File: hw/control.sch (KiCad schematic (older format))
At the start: 12 parts

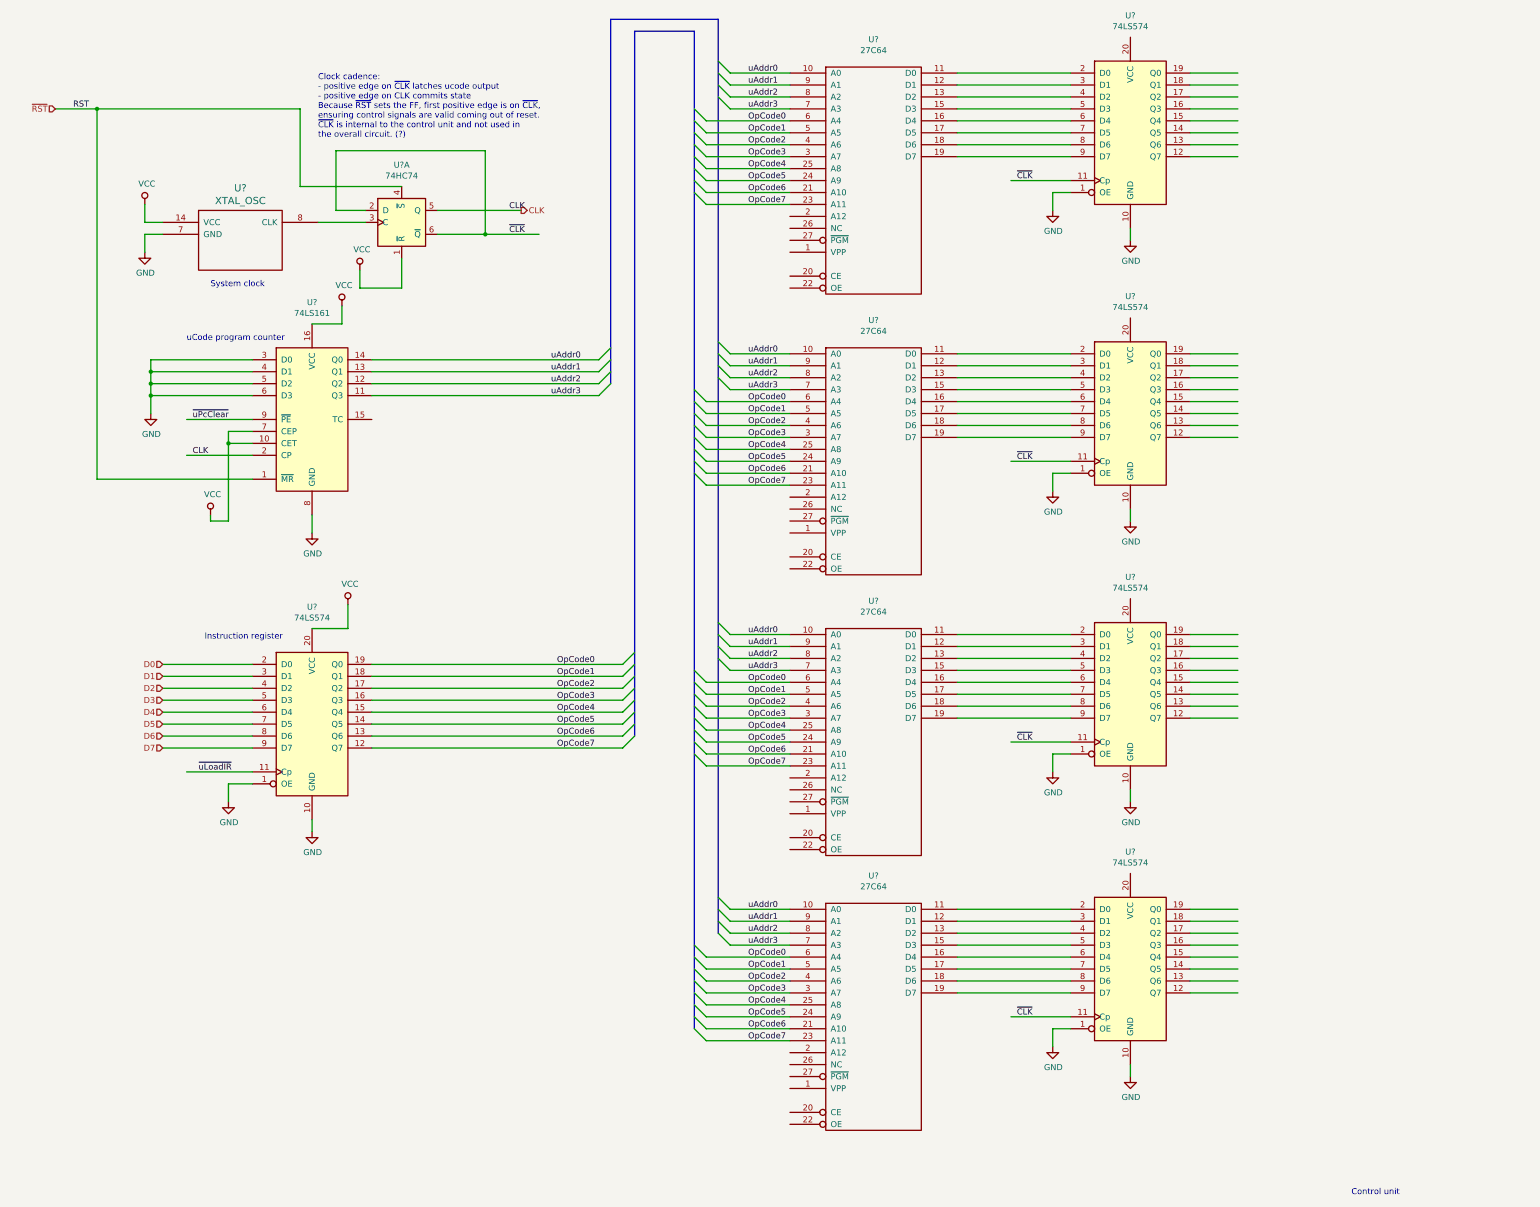
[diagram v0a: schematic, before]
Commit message: annotate control schematic, add other 74HC74 units
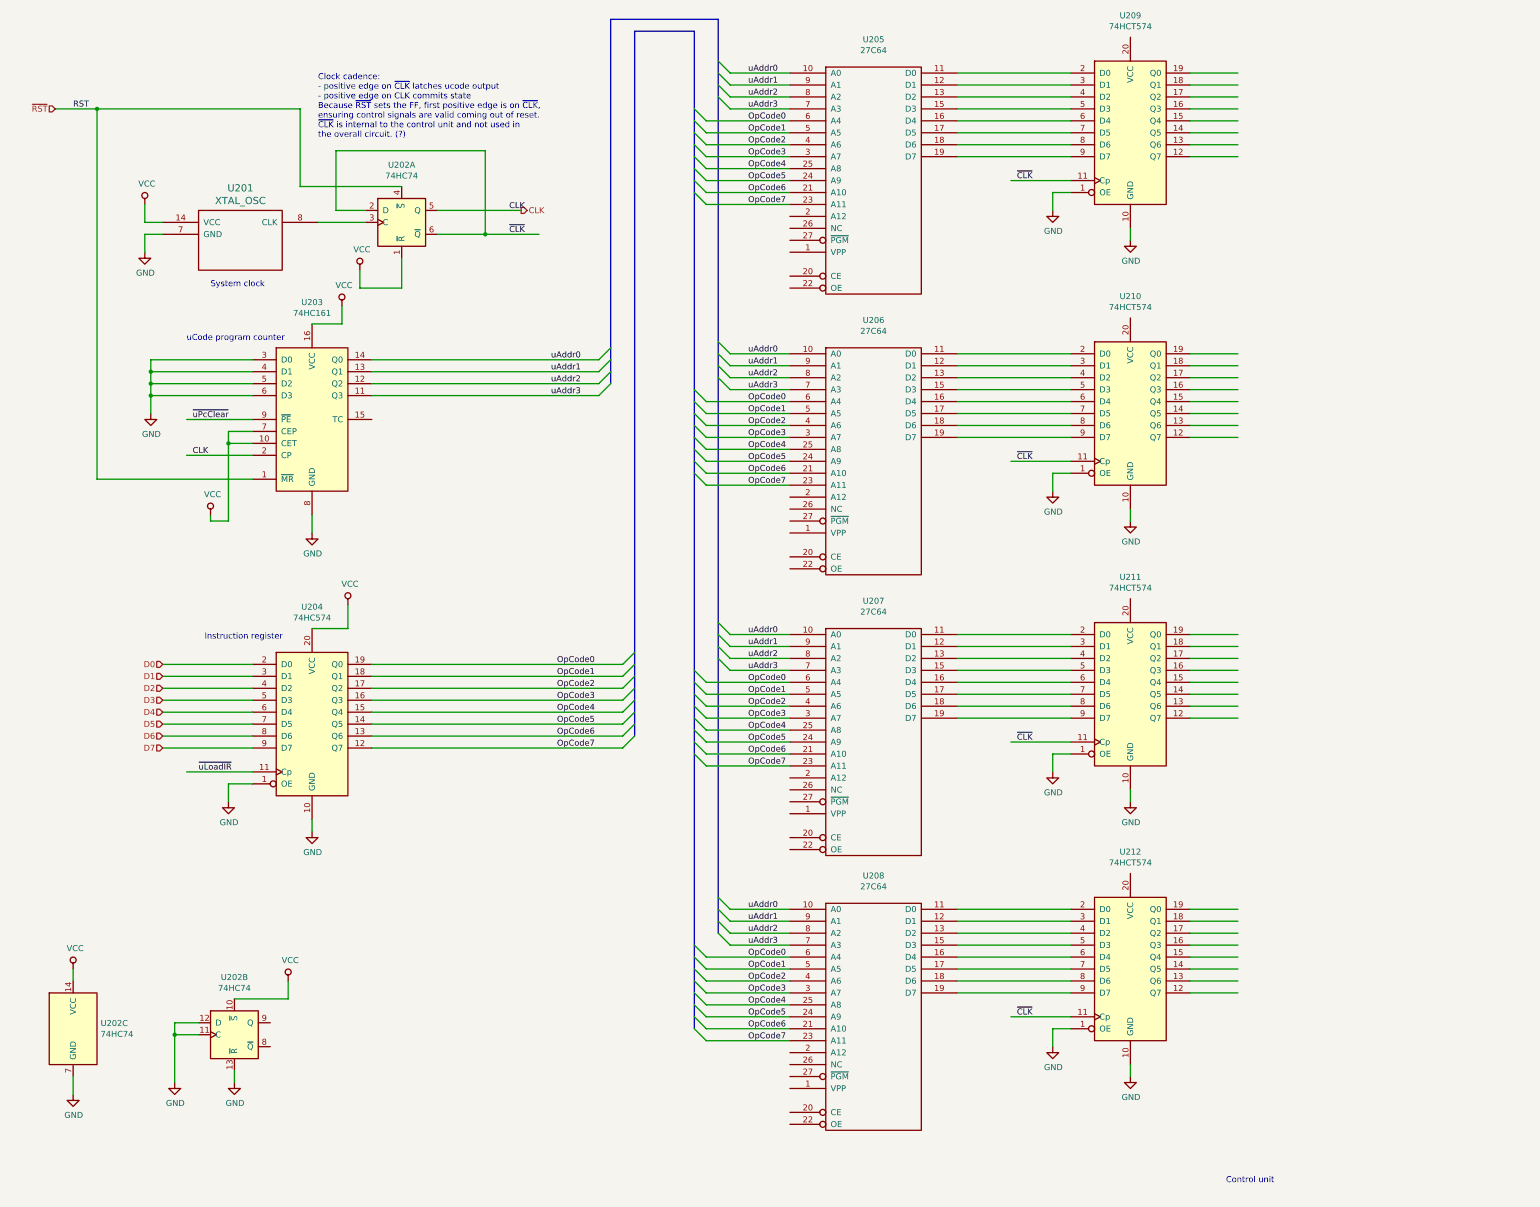
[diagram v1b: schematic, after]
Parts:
- added unit 2 of U202
- added unit 3 of U202
- U203: renamed from U?; value 74LS161 -> 74HC161
- U204: renamed from U?; value 74LS574 -> 74HC574
- U209, U210, U211, U212: renamed from U?; value 74LS574 -> 74HCT574
- gave numbers to parts that had none: 6
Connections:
- wire segments 194 -> 203
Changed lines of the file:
@@
 EELAYER 30 0
 EELAYER END
-$Descr User 16500 12750
+$Descr User 15400 11900
 encoding utf-8
 Sheet 3 3
@@
 $EndDescr
 $Comp
-L 74xx:74LS161 U?
+L 74xx:74LS161 U203
 U 1 1 5DA2ED38
 P 3150 3950
-F 0 "U?" H 3150 4931 50  0000 C CNN
-F 1 "74LS161" H 3150 4840 50  0000 C CNN
+F 0 "U203" H 3150 4931 50  0000 C CNN
+F 1 "74HC161" H 3150 4840 50  0000 C CNN
 F 2 "" H 3150 3950 50  0001 C CNN
 F 3 "" H 3150 3950 50  0001 C CNN
@@
 $EndComp
 $Comp
-L ya68k:XTAL_OSC U?
+L ya68k:XTAL_OSC U201
 U 1 1 5DA2F9CD
 P 2550 2450
-F 0 "U?" H 2550 2887 60  0000 C CNN
+F 0 "U201" H 2550 2887 60  0000 C CNN
 F 1 "XTAL_OSC" H 2550 2781 60  0000 C CNN
 F 2 "" H 2550 2450 60  0000 C CNN
@@
 $EndComp
 $Comp
-L 74xx:74HC74 U?
+L 74xx:74HC74 U202
 U 1 1 5DA3008F
 P 3900 2300
-F 0 "U?" H 3900 2781 50  0000 C CNN
+F 0 "U202" H 3900 2781 50  0000 C CNN
 F 1 "74HC74" H 3900 2690 50  0000 C CNN
 F 2 "" H 3900 2300 50  0001 C CNN
@@
 	1    0    0    -1
 $EndComp
-Text Notes 11850 10450 0    50   ~ 0
+Text Notes 10800 10350 0    50   ~ 0
 Control unit
 Wire Wire Line
@@
 uAddr3
 $Comp
-L memory:27C64 U?
+L memory:27C64 U205
 U 1 1 5DA55452
 P 7850 1950
-F 0 "U?" H 7850 3131 50  0000 C CNN
+F 0 "U205" H 7850 3131 50  0000 C CNN
 F 1 "27C64" H 7850 3040 50  0000 C CNN
 F 2 "" H 7850 1950 50  0001 C CNN
@@
 Instruction register
 $Comp
-L 74xx:74LS574 U?
+L 74xx:74LS574 U204
 U 1 1 5DA56DCA
 P 3150 6500
-F 0 "U?" H 3150 7481 50  0000 C CNN
-F 1 "74LS574" H 3150 7390 50  0000 C CNN
+F 0 "U204" H 3150 7481 50  0000 C CNN
+F 1 "74HC574" H 3150 7390 50  0000 C CNN
 F 2 "" H 3150 6500 50  0001 C CNN
 F 3 "" H 3150 6500 50  0001 C CNN
@@
 	5750 6700 5850 6600
 $Comp
-L memory:27C64 U?
+L memory:27C64 U206
 U 1 1 5DB46557
 P 7850 4300
-F 0 "U?" H 7850 5481 50  0000 C CNN
+F 0 "U206" H 7850 5481 50  0000 C CNN
 F 1 "27C64" H 7850 5390 50  0000 C CNN
 F 2 "" H 7850 4300 50  0001 C CNN
@@
 	6350 4400 6450 4500
 $Comp
-L memory:27C64 U?
+L memory:27C64 U207
 U 1 1 5DBB547A
 P 7850 6650
-F 0 "U?" H 7850 7831 50  0000 C CNN
+F 0 "U207" H 7850 7831 50  0000 C CNN
 F 1 "27C64" H 7850 7740 50  0000 C CNN
 F 2 "" H 7850 6650 50  0001 C CNN
@@
 OpCode7
 $Comp
-L memory:27C64 U?
+L memory:27C64 U208
 U 1 1 5DBB54A8
 P 7850 8950
-F 0 "U?" H 7850 10131 50  0000 C CNN
+F 0 "U208" H 7850 10131 50  0000 C CNN
 F 1 "27C64" H 7850 10040 50  0000 C CNN
 F 2 "" H 7850 8950 50  0001 C CNN
@@
 	6350 9050 6450 9150
 $Comp
-L 74xx:74LS574 U?
+L 74xx:74LS574 U209
 U 1 1 5DBF0B9D
 P 10000 1550
-F 0 "U?" H 10000 2531 50  0000 C CNN
-F 1 "74LS574" H 10000 2440 50  0000 C CNN
+F 0 "U209" H 10000 2531 50  0000 C CNN
+F 1 "74HCT574" H 10000 2440 50  0000 C CNN
 F 2 "" H 10000 1550 50  0001 C CNN
 F 3 "" H 10000 1550 50  0001 C CNN
@@
 	10500 1750 10900 1750
 $Comp
-L 74xx:74LS574 U?
+L 74xx:74LS574 U210
 U 1 1 5DC59E56
 P 10000 3900
-F 0 "U?" H 10000 4881 50  0000 C CNN
-F 1 "74LS574" H 10000 4790 50  0000 C CNN
+F 0 "U210" H 10000 4881 50  0000 C CNN
+F 1 "74HCT574" H 10000 4790 50  0000 C CNN
 F 2 "" H 10000 3900 50  0001 C CNN
 F 3 "" H 10000 3900 50  0001 C CNN
@@
 	10500 4100 10900 4100
 $Comp
-L 74xx:74LS574 U?
+L 74xx:74LS574 U211
 U 1 1 5DC7146C
 P 10000 6250
-F 0 "U?" H 10000 7231 50  0000 C CNN
-F 1 "74LS574" H 10000 7140 50  0000 C CNN
+F 0 "U211" H 10000 7231 50  0000 C CNN
+F 1 "74HCT574" H 10000 7140 50  0000 C CNN
 F 2 "" H 10000 6250 50  0001 C CNN
 F 3 "" H 10000 6250 50  0001 C CNN
@@
 	10500 6450 10900 6450
 $Comp
-L 74xx:74LS574 U?
+L 74xx:74LS574 U212
 U 1 1 5DC8BA8C
 P 10000 8550
-F 0 "U?" H 10000 9531 50  0000 C CNN
-F 1 "74LS574" H 10000 9440 50  0000 C CNN
+F 0 "U212" H 10000 9531 50  0000 C CNN
+F 1 "74HCT574" H 10000 9440 50  0000 C CNN
 F 2 "" H 10000 8550 50  0001 C CNN
 F 3 "" H 10000 8550 50  0001 C CNN
@@
 Wire Wire Line
 	10500 8750 10900 8750
+$Comp
+L 74xx:74HC74 U202
+U 2 1 5DA52673
+P 2500 9100
+F 0 "U202" H 2500 9581 50  0000 C CNN
+F 1 "74HC74" H 2500 9490 50  0000 C CNN
+F 2 "" H 2500 9100 50  0001 C CNN
+F 3 "" H 2500 9100 50  0001 C CNN
+	2    2500 9100
+	1    0    0    -1
+$EndComp
+$Comp
+L 74xx:74HC74 U202
+U 3 1 5DA537B9
+P 1150 9050
+F 0 "U202" H 1380 9096 50  0000 L CNN
+F 1 "74HC74" H 1380 9005 50  0000 L CNN
+F 2 "" H 1150 9050 50  0001 C CNN
+F 3 "" H 1150 9050 50  0001 C CNN
+	3    1150 9050
+	1    0    0    -1
+$EndComp
+Wire Wire Line
+	1150 8650 1150 8550
+$Comp
+L power:VCC #PWR?
+U 1 1 5DA7BA20
+P 1150 8550
+F 0 "#PWR?" H 1150 8400 50  0001 C CNN
+F 1 "VCC" H 1167 8723 50  0000 C CNN
+F 2 "" H 1150 8550 50  0001 C CNN
+F 3 "" H 1150 8550 50  0001 C CNN
+	1    1150 8550
+	1    0    0    -1
+$EndComp
+Wire Wire Line
+	1150 9450 1150 9600
+$Comp
+L power:GND #PWR?
+U 1 1 5DA88242
+P 1150 9600
+F 0 "#PWR?" H 1150 9350 50  0001 C CNN
+F 1 "GND" H 1155 9427 50  0000 C CNN
+F 2 "" H 1150 9600 50  0001 C CNN
+F 3 "" H 1150 9600 50  0001 C CNN
+	1    1150 9600
+	1    0    0    -1
+$EndComp
+Wire Wire Line
+	2200 9000 2000 9000
+Wire Wire Line
+	2000 9000 2000 9100
+Wire Wire Line
+	2200 9100 2000 9100
+Connection ~ 2000 9100
+Wire Wire Line
+	2000 9100 2000 9500
+Wire Wire Line
+	2500 8800 2950 8800
+Wire Wire Line
+	2950 8800 2950 8650
+Wire Wire Line
+	2500 9400 2500 9500
+$Comp
+L power:VCC #PWR?
+U 1 1 5DABCB90
+P 2950 8650
+F 0 "#PWR?" H 2950 8500 50  0001 C CNN
+F 1 "VCC" H 2967 8823 50  0000 C CNN
+F 2 "" H 2950 8650 50  0001 C CNN
+F 3 "" H 2950 8650 50  0001 C CNN
+	1    2950 8650
+	1    0    0    -1
+$EndComp
+$Comp
+L power:GND #PWR?
+U 1 1 5DABD30A
+P 2500 9500
+F 0 "#PWR?" H 2500 9250 50  0001 C CNN
+F 1 "GND" H 2505 9327 50  0000 C CNN
+F 2 "" H 2500 9500 50  0001 C CNN
+F 3 "" H 2500 9500 50  0001 C CNN
+	1    2500 9500
+	1    0    0    -1
+$EndComp
 Wire Bus Line
 	5650 600  5650 3650
@@
 Wire Bus Line
 	6350 700  6350 9050
+$Comp
+L power:GND #PWR?
+U 1 1 5DACABB5
+P 2000 9500
+F 0 "#PWR?" H 2000 9250 50  0001 C CNN
+F 1 "GND" H 2005 9327 50  0000 C CNN
+F 2 "" H 2000 9500 50  0001 C CNN
+F 3 "" H 2000 9500 50  0001 C CNN
+	1    2000 9500
+	1    0    0    -1
+$EndComp
 $EndSCHEMATC

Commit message: added reset unit, some cleanups of control unit
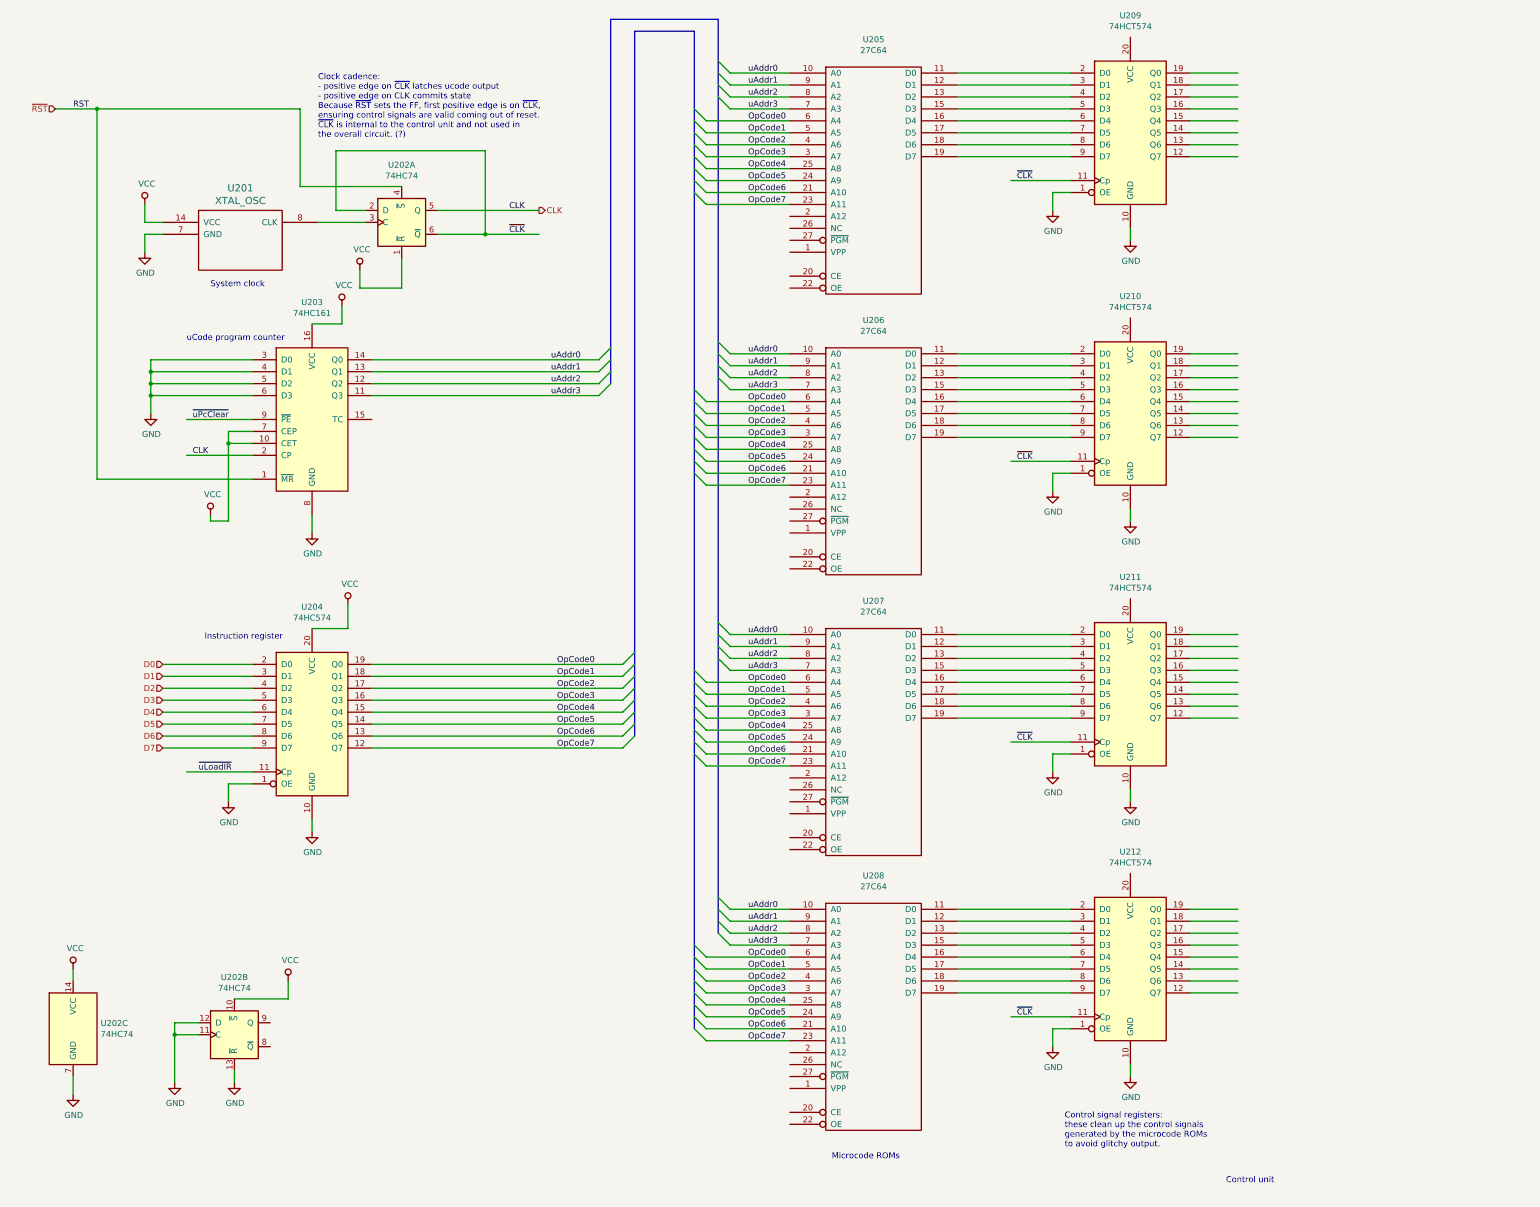
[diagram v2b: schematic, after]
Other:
- note added: "Control signal registers:\nthese clean up the control signals\ngenerated by the microcode ROMs\nto avoid glitchy output."
- note added: "Microcode ROMs"
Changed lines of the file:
@@
 $Descr User 15400 11900
 encoding utf-8
-Sheet 3 3
+Sheet 3 4
 Title ""
 Date ""
@@
 System clock
 Wire Wire Line
-	4200 2200 4900 2200
+	4200 2200 5050 2200
 Wire Wire Line
 	5050 2400 4600 2400
 Connection ~ 4600 2400
-Text HLabel 4900 2200 2    50   Output ~ 0
+Text HLabel 5050 2200 2    50   Output ~ 0
 CLK
 Text Label 4800 2200 0    50   ~ 0
@@
 	1    0    0    -1
 $EndComp
+$Comp
+L power:GND #PWR?
+U 1 1 5DACABB5
+P 2000 9500
+F 0 "#PWR?" H 2000 9250 50  0001 C CNN
+F 1 "GND" H 2005 9327 50  0000 C CNN
+F 2 "" H 2000 9500 50  0001 C CNN
+F 3 "" H 2000 9500 50  0001 C CNN
+	1    2000 9500
+	1    0    0    -1
+$EndComp
+Text Notes 7500 10150 0    50   ~ 0
+Microcode ROMs
+Text Notes 9450 10050 0    50   ~ 0
+Control signal registers:\nthese clean up the control signals\ngenerated by the microcode ROMs\nto avoid glitchy output.
 Wire Bus Line
 	5650 600  5650 3650
@@
 Wire Bus Line
 	6350 700  6350 9050
-$Comp
-L power:GND #PWR?
-U 1 1 5DACABB5
-P 2000 9500
-F 0 "#PWR?" H 2000 9250 50  0001 C CNN
-F 1 "GND" H 2005 9327 50  0000 C CNN
-F 2 "" H 2000 9500 50  0001 C CNN
-F 3 "" H 2000 9500 50  0001 C CNN
-	1    2000 9500
-	1    0    0    -1
-$EndComp
 $EndSCHEMATC
